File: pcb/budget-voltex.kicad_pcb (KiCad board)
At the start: 2 copper layers, 225.1 x 135.7 mm, 19 parts

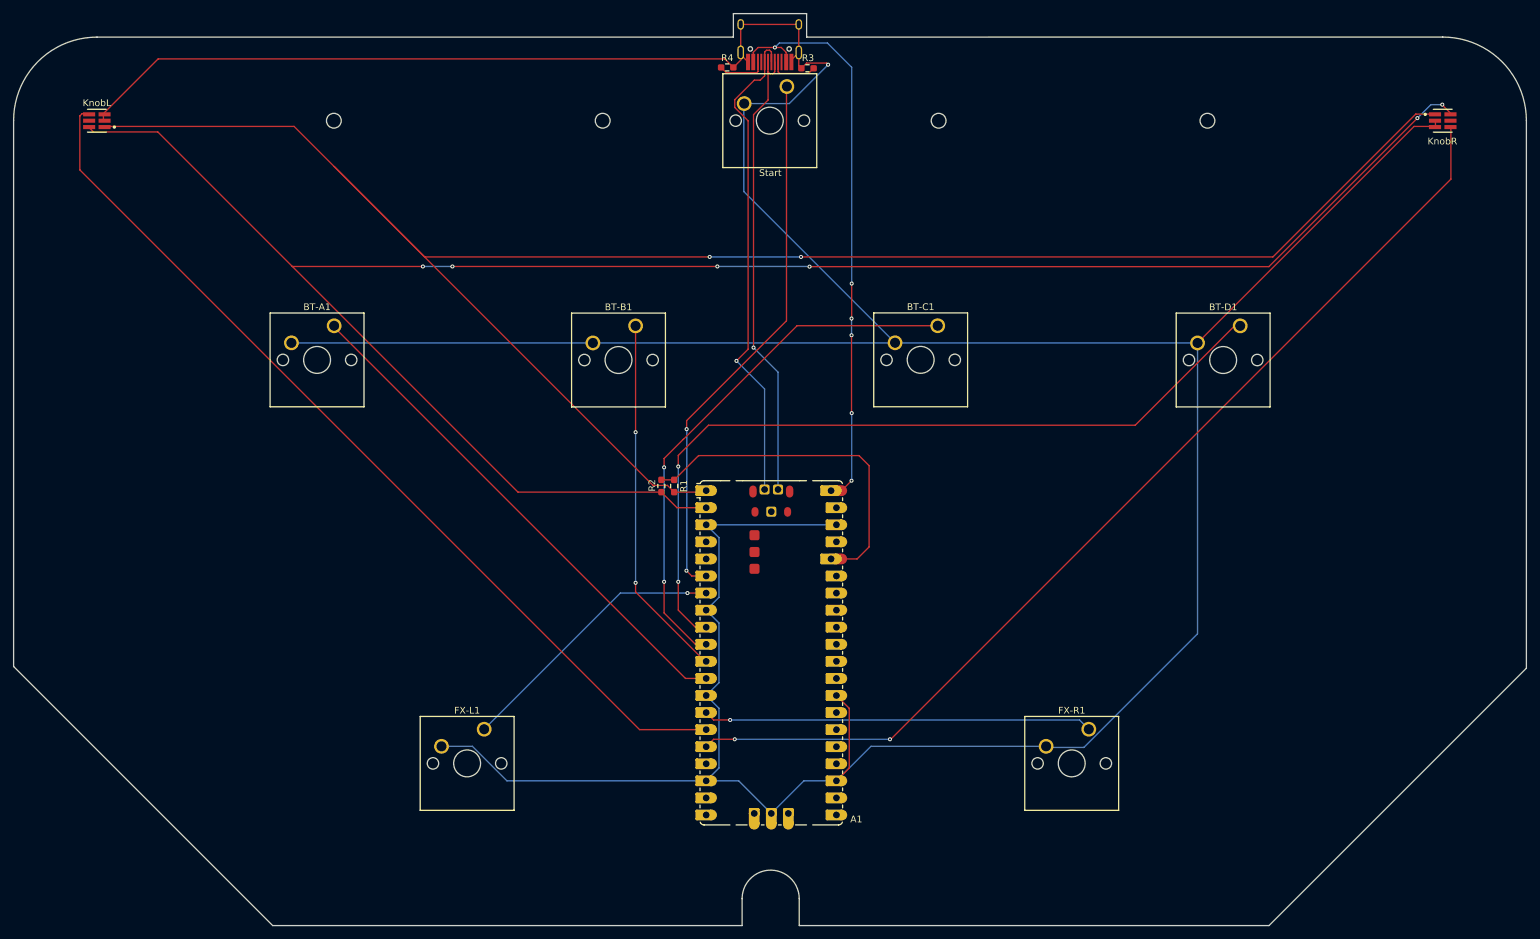
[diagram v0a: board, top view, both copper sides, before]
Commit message: Updated key footprints to use chocs, rewire everything
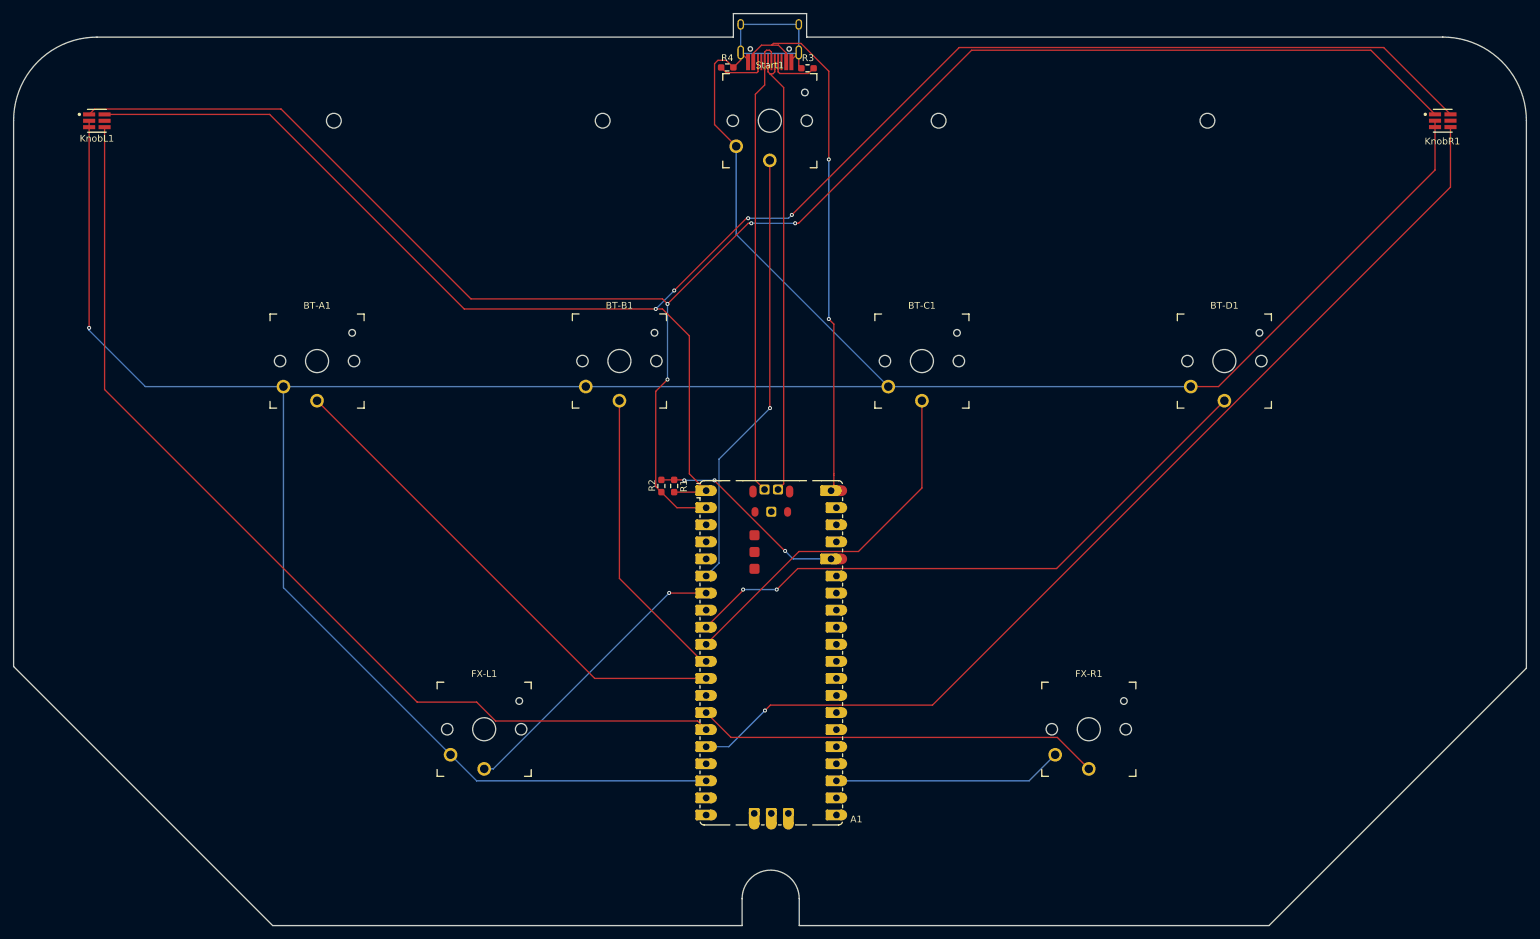
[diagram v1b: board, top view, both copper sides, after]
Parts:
- BT-A1, BT-B1, BT-C1, BT-D1, FX-L1, FX-R1: footprint Button_Switch_Keyboard:SW_Cherry_MX_1.00u_PCB -> keyswitches:SW_PG1350
- Start1: renamed from Start; footprint Button_Switch_Keyboard:SW_Cherry_MX_1.00u_PCB -> keyswitches:SW_PG1350
- moved BT-A1 5.83 mm to (84.4, 84.0)
- moved BT-C1 5.77 mm to (174.4, 84.0)
- moved BT-B1 5.75 mm to (129.3, 84.0)
- moved BT-D1 5.74 mm to (219.4, 84.0)
- moved Start1 5.69 mm to (151.7, 48.2)
- turned KnobL1 to 0 degrees
- renumbered KnobL to KnobL1, KnobR to KnobR1
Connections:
- A1 pad : +3V3 -> (no net)
- KnobL1 pad 1: SDA -> SCL
- KnobL1 pad 6: SCL -> SDA
- KnobR1 pad 1: SDA -> SCL
- KnobR1 pad 6: SCL -> SDA
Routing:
- net GND: track 620.9 -> 491.4 mm
- net SCL: track 298.5 -> 268.9 mm, vias 6 -> 4
- net Net-(A1-GPIO6): track 119.8 -> 91.1 mm
- net Net-(A1-GPIO7): track 80.1 -> 54.7 mm, vias 2 -> 0
- net SDA: track 290.5 -> 268.1 mm, vias 2 -> 4
- net +3V3: track 49.6 -> 30.1 mm, vias 0 -> 3
- net Net-(A1-GPIO4): track 81.6 -> 65.8 mm, vias 2 -> 1
- net Net-(A1-GPIO11): track 137.1 -> 149.5 mm
- net Net-(A1-GPIO8): track 54.4 -> 44.5 mm, vias 2 -> 0
- net Net-(A1-USB_DP): track 73.4 -> 68.9 mm, vias 1 -> 0
- net Net-(A1-GPIO5): track 41.4 -> 43.9 mm
- net Net-(A1-GPIO10): track 58.0 -> 60.4 mm, vias 1 -> 0
- net Net-(A1-VBUS): track 85.1 -> 82.7 mm, vias 6 -> 2
- net Net-(A1-GPIO9): track 77.3 -> 75.0 mm
- net Net-(A1-USB_DM): track 68.7 -> 67.2 mm, vias 1 -> 0
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
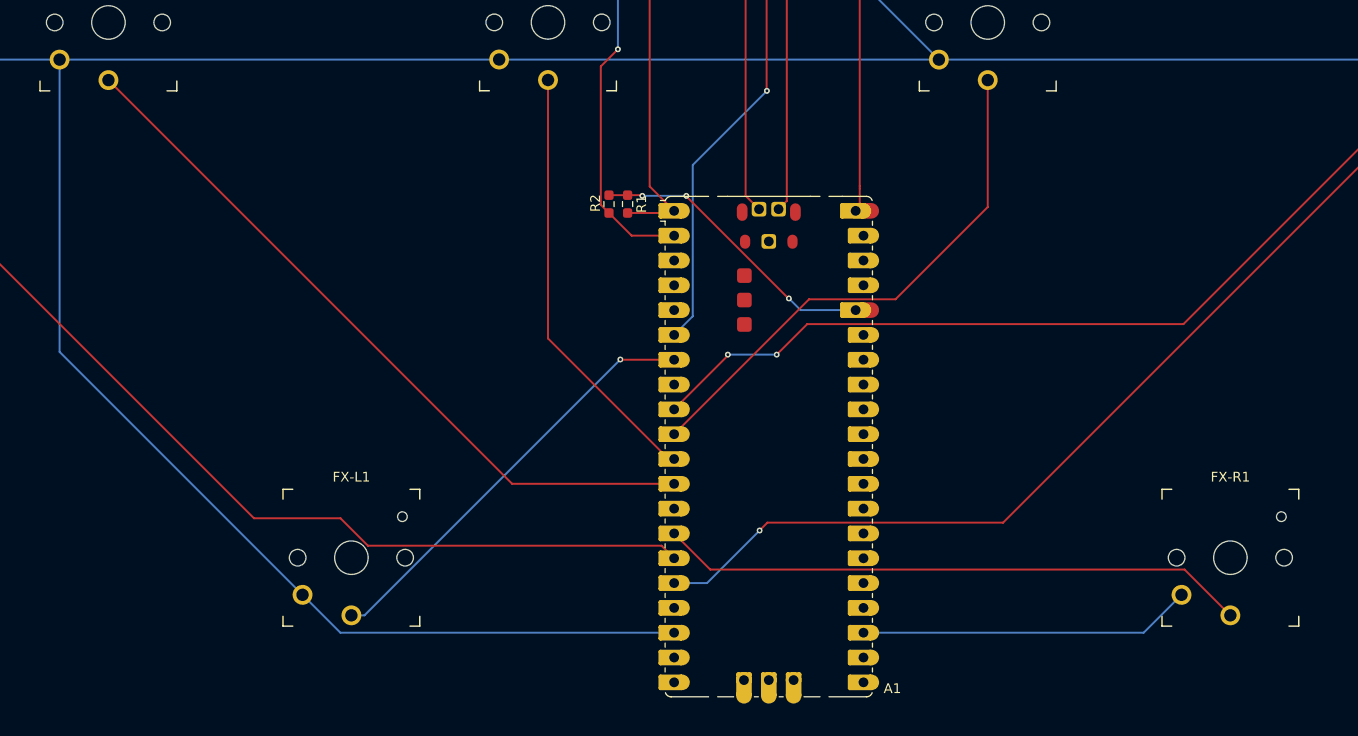
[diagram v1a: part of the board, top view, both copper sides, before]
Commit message: Fix positioning of fx buttons
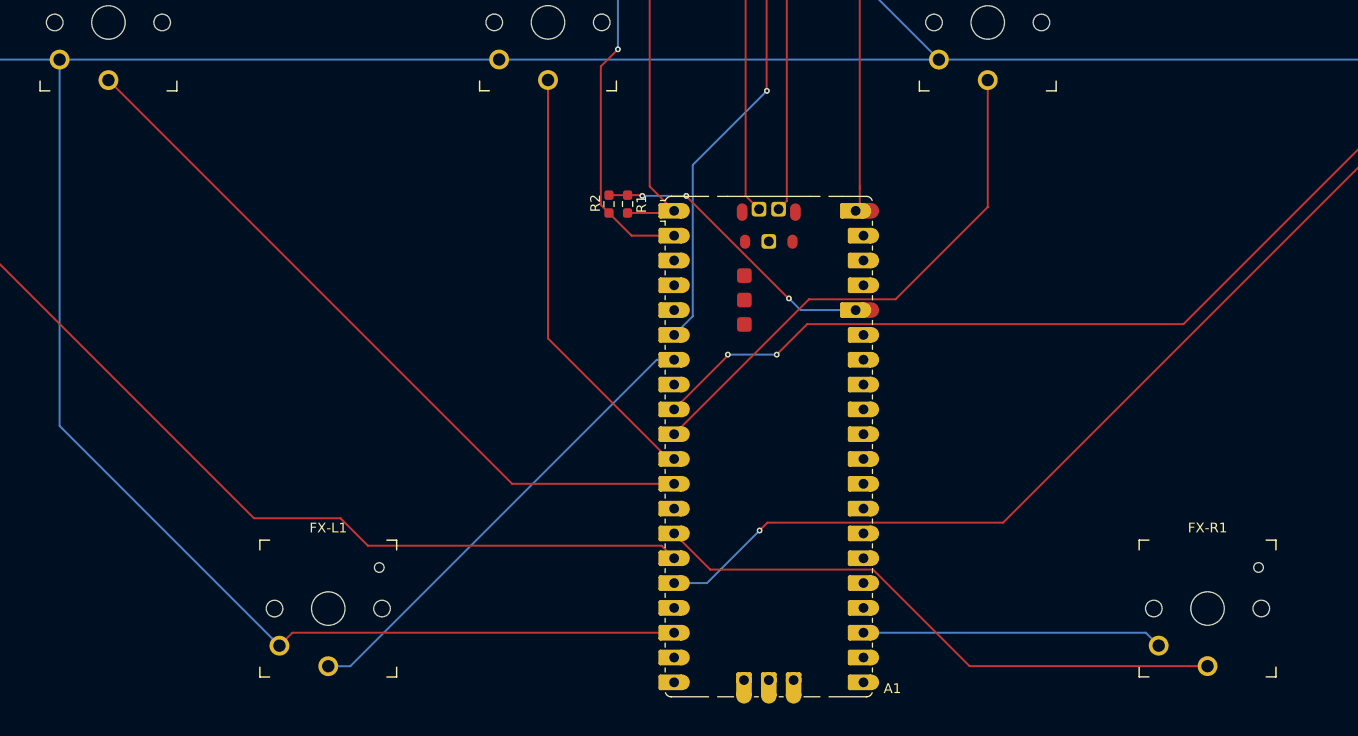
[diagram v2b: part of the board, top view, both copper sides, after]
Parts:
- moved FX-L1 5.72 mm to (106.9, 144.0)
- moved FX-R1 5.70 mm to (196.9, 144.0)
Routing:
- net Net-(A1-GPIO5): track 43.9 -> 48.4 mm, vias 1 -> 0
- net GND: track 491.4 -> 493.5 mm
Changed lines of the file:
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@@
 	(footprint "keyswitches:SW_PG1350"
 		(layer "F.Cu")
-		(at 199.1868 138.7856)
+		(at 196.850541 143.986759)
 		(descr "Kailh \"Choc\" PG1350 keyswitch")
 		(tags "kailh,choc")
@@
 	(footprint "keyswitches:SW_PG1350"
 		(layer "F.Cu")
-		(at 109.22 138.7856)
+		(at 106.852957 143.992985)
 		(descr "Kailh \"Choc\" PG1350 keyswitch")
 		(tags "kailh,choc")
@@
 	)
 	(segment
-		(start 194.5012 140)
-		(end 145.9495 140)
+		(start 145.9495 140)
+		(end 142.2528 136.3033)
 		(width 0.2)
 		(layer "F.Cu")
@@
 	)
 	(segment
-		(start 145.9495 140)
-		(end 142.2528 136.3033)
+		(start 196.850541 149.886759)
+		(end 172.500381 149.886759)
 		(width 0.2)
 		(layer "F.Cu")
@@
 	)
 	(segment
-		(start 199.1868 144.6856)
-		(end 194.5012 140)
+		(start 162.613622 140)
+		(end 145.9495 140)
+		(width 0.2)
+		(layer "F.Cu")
+		(net 9)
+	)
+	(segment
+		(start 172.500381 149.886759)
+		(end 162.613622 140)
 		(width 0.2)
 		(layer "F.Cu")
@@
 	)
 	(segment
+		(start 103.182642 146.4633)
+		(end 142.2528 146.4633)
+		(width 0.2)
+		(layer "F.Cu")
+		(net 15)
+	)
+	(segment
 		(start 218.481654 87.79999)
 		(end 214.360596 87.79999)
@@
 	)
 	(segment
+		(start 101.852957 147.792985)
+		(end 103.182642 146.4633)
+		(width 0.2)
+		(layer "F.Cu")
+		(net 15)
+	)
+	(segment
 		(start 147.3902 39.2217)
 		(end 146.3021 40.3098)
@@
 	)
 	(segment
-		(start 104.22 142.5856)
-		(end 108.0977 146.4633)
-		(width 0.2)
-		(layer "B.Cu")
-		(net 15)
-	)
-	(segment
 		(start 146.720495 52.0378)
 		(end 146.720495 65.169889)
@@
 	)
 	(segment
-		(start 104.22 142.5856)
-		(end 79.352957 117.718557)
-		(width 0.2)
-		(layer "B.Cu")
-		(net 15)
-	)
-	(segment
 		(start 147.3902 33.9052)
 		(end 156.0302 33.9052)
@@
 	)
 	(segment
-		(start 190.3091 146.4633)
-		(end 194.1868 142.5856)
-		(width 0.2)
-		(layer "B.Cu")
-		(net 15)
-	)
-	(segment
 		(start 79.352957 87.802893)
 		(end 214.357693 87.802893)
@@
 	)
 	(segment
-		(start 108.0977 146.4633)
-		(end 142.2528 146.4633)
-		(width 0.2)
-		(layer "B.Cu")
-		(net 15)
-	)
-	(segment
 		(start 147.3902 33.9052)
 		(end 147.3902 38.0852)
@@
 	)
 	(segment
-		(start 161.6328 146.4633)
-		(end 190.3091 146.4633)
+		(start 79.352957 87.802893)
+		(end 79.352957 125.292985)
 		(width 0.2)
 		(layer "B.Cu")
@@
 	)
 	(segment
-		(start 79.352957 117.718557)
-		(end 79.352957 87.802893)
+		(start 50.436917 79.063083)
+		(end 50.436917 79.436917)
 		(width 0.2)
 		(layer "B.Cu")
@@
 	)
 	(segment
-		(start 50.436917 79.063083)
-		(end 50.436917 79.436917)
+		(start 190.527082 146.4633)
+		(end 161.6328 146.4633)
 		(width 0.2)
 		(layer "B.Cu")
@@
 	)
 	(segment
+		(start 191.850541 147.786759)
+		(end 190.527082 146.4633)
+		(width 0.2)
+		(layer "B.Cu")
+		(net 15)
+	)
+	(segment
+		(start 79.352957 125.292985)
+		(end 101.852957 147.792985)
+		(width 0.2)
+		(layer "B.Cu")
+		(net 15)
+	)
+	(segment
 		(start 146.720495 65.169889)
 		(end 169.353525 87.802919)
@@
 	)
 	(segment
-		(start 136.7733 118.5233)
-		(end 142.2528 118.5233)
-		(width 0.2)
-		(layer "F.Cu")
-		(net 31)
-	)
-	(segment
-		(start 136.75 118.5)
-		(end 136.7733 118.5233)
+		(start 109.107015 149.892985)
+		(end 140.4767 118.5233)
 		(width 0.2)
-		(layer "F.Cu")
-		(net 31)
-	)
-	(via
-		(at 136.75 118.5)
-		(size 0.6)
-		(drill 0.3)
-		(layers "F.Cu" "B.Cu")
+		(layer "B.Cu")
 		(net 31)
 	)
 	(segment
-		(start 109.22 144.6856)
-		(end 110.5644 144.6856)
+		(start 106.852957 149.892985)
+		(end 109.107015 149.892985)
 		(width 0.2)
 		(layer "B.Cu")
@@
 	)
 	(segment
-		(start 110.5644 144.6856)
-		(end 136.75 118.5)
+		(start 140.4767 118.5233)
+		(end 142.2528 118.5233)
 		(width 0.2)
 		(layer "B.Cu")

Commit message: Idk what i did
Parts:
- A1: footprint Module:RaspberryPi_Pico_SMD -> minnowfeather-custom-fp:RaspberryPi_Pico_SMD_Modified
